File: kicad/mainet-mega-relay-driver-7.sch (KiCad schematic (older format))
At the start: 8 parts, among them J36 Screw_Terminal_01x03, K7 SANYOU_SRD_Form_C, Q7 2N3904, U8 4N37

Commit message: KICAD: Actualizar archivos del módulo de relés
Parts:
- added J91, J92: Conn_01x01_Male, symbol Connector:Conn_01x01_Male
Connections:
- net C7 renamed brakeChunkActivation
- net brakeChunkActivation: now also J92.1 (Pin_1)
- net NO7 renamed +24V
- net +24V: now also J91.1 (Pin_1)
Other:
- note added: "Activación de la válvula solenoide,\n2 posiciones simple,\ndel "chunk" del freno"
- note added: "Relay Ground\nNo conectar a la tierra\ndel Arduino Mega\n"
- note removed: "No conectar a la tierra del Arduino Mega\n"
- note removed: "Relay Ground\n"
- moved on the sheet: D13, D14, J36, K7, Q7, R13, R14, U8

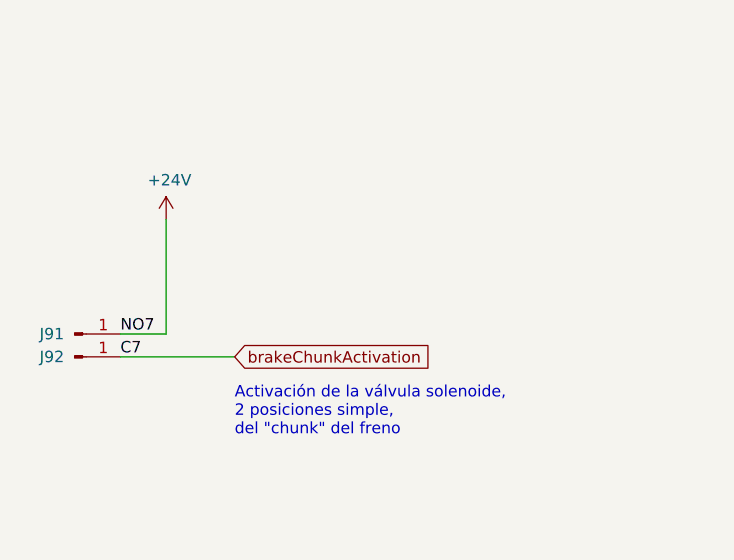
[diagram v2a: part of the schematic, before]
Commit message: KICAD: Agregar cambios esquemáticos
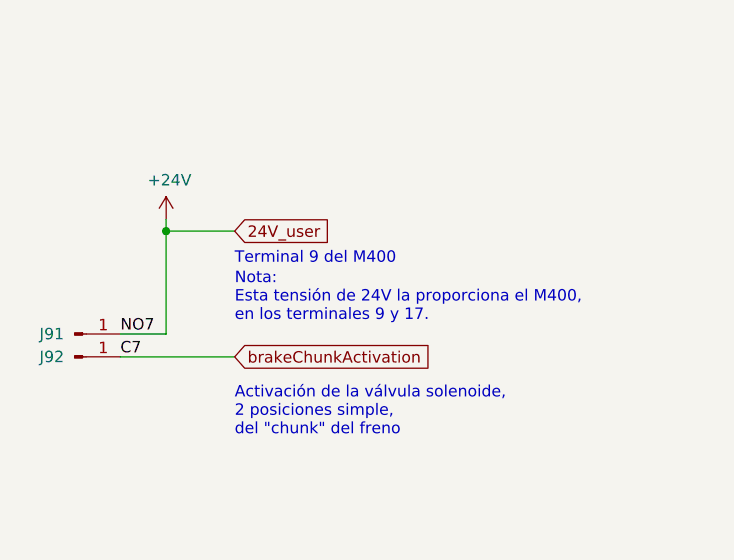
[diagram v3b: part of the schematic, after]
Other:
- note added: "Nota:\nEsta tensión de 24V la proporciona el M400, \nen los terminales 9 y 17."
- note added: "Terminal 9 del M400"
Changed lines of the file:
@@
 Sheet 13 22
 Title "Mainet-mega -- brakeChunkControl"
-Date "2021-04-07"
+Date "2021-06-18"
 Rev "1.0"
 Comp "Tovenca"
@@
 $EndComp
 Wire Wire Line
-	8300 3200 8300 3700
+	8300 3200 8300 3250
 Wire Wire Line
 	8300 3700 8100 3700
@@
 Text Notes 2950 3800 0    50   ~ 0
 Relay Ground\nNo conectar a la tierra\ndel Arduino Mega\n
+Text GLabel 8600 3250 2    50   Input ~ 0
+24V_user
+Wire Wire Line
+	8300 3250 8600 3250
+Text Notes 8600 3400 0    50   ~ 0
+Terminal 9 del M400
+Text Notes 8600 3650 0    50   ~ 0
+Nota:\nEsta tensión de 24V la proporciona el M400, \nen los terminales 9 y 17.
+Connection ~ 8300 3250
+Wire Wire Line
+	8300 3250 8300 3700
 $EndSCHEMATC

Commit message: KICAD: Actualizar .sch chunk del freno
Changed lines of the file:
@@
 Sheet 13 22
 Title "Mainet-mega -- brakeChunkControl"
-Date "2021-06-18"
+Date "2021-07-14"
 Rev "1.0"
 Comp "Tovenca"
@@
 Relay Ground\nNo conectar a la tierra\ndel Arduino Mega\n
 Text GLabel 8600 3250 2    50   Input ~ 0
-24V_user
++24V
 Wire Wire Line
 	8300 3250 8600 3250
